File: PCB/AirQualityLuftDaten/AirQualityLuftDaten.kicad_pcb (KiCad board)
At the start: 2 copper layers, 69.9 x 69.9 mm, 21 parts, among them J1 5V_DC_JACK, J10 I2C_2, J11 I2C_3, J12 DHT22, J13 SDS011, J14 ESP_BO1, J15 ESP_BO2, J16 LOGO_LUFTDATEN, J17 LOGO_AirRohr, J18 LOGO_TCEC, J2 5V_POWER, J3 ADC_IN, J4 ADAFRUIT_ADS1115_ADC, J5 PCB, J6 LOGO_OSW, J7 LOGO_TCEC, J8 BME280, J9 I2C_1, P1 5V_USB_Micro, U1 NODEMCU

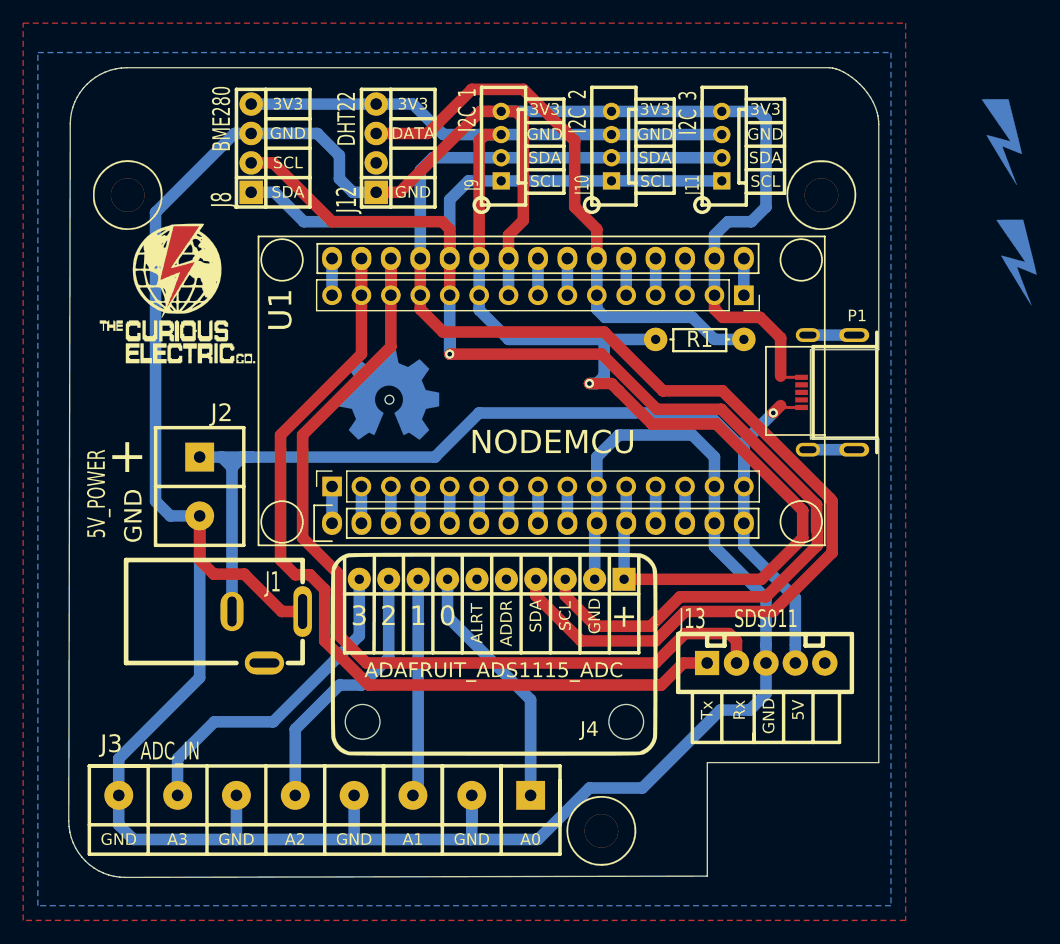
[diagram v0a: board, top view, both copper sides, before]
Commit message: Updated PCB and baseplate files
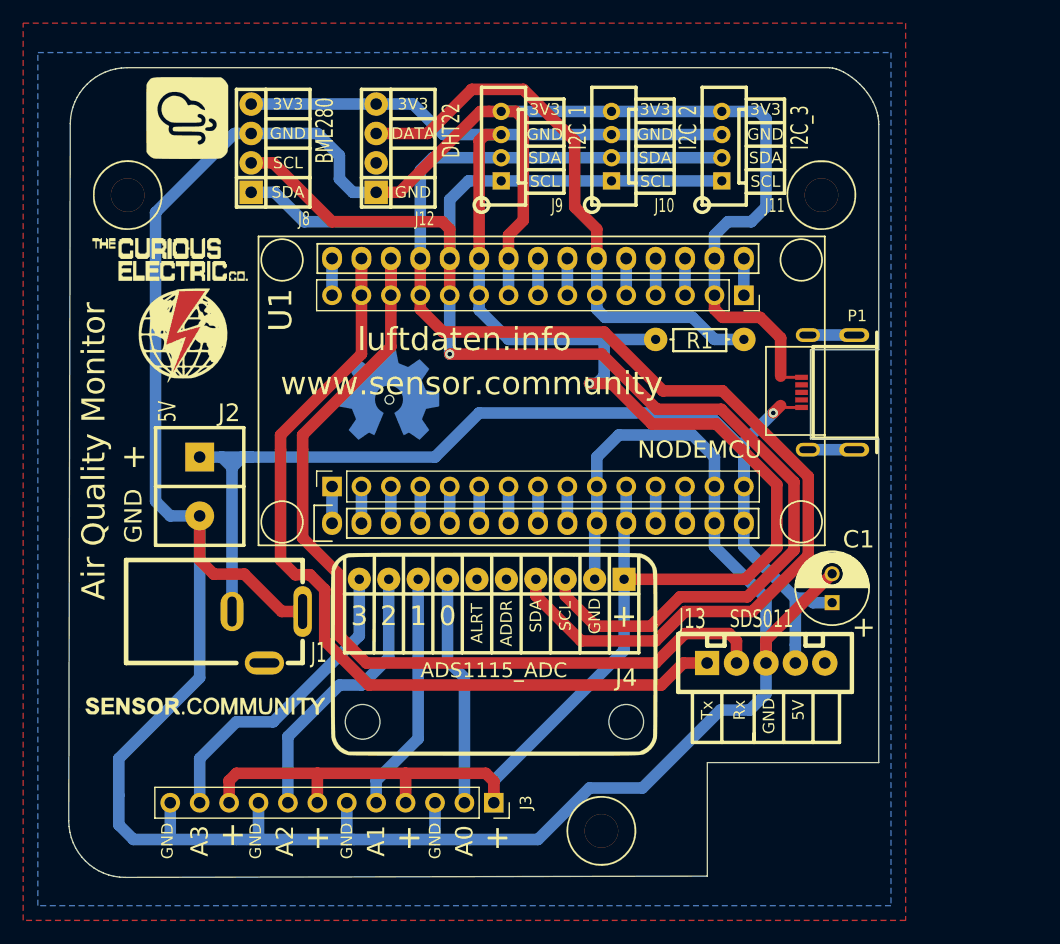
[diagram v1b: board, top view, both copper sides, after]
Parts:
- added C1: 100uf, REInnovationFootprint:C_Radial_D6.3_L11.2_P2.5, F.Cu at (171.4, 105.9)
- J1: value 5V_DC_JACK -> 5V
- J16: footprint CuriousElectric3:2019_011_16_CuriousElectricCompany_Logo_Round_Logo_No_words_KiCAD_10mm_PCBLogo -> CuriousElectric3:sensorcommunity
- J17: footprint CuriousElectric3:2019_011_16_CuriousElectricCompany_Logo_Round_Logo_No_words_KiCAD_10mm_PCBLogo -> CuriousElectric3:logo_conversion
- J2: value 5V_POWER -> 5V
- J3: footprint REInnovationFootprint:SIL_8_Screw_AIO -> REInnovationFootprint:PinSocket_1x12_P2.54mm_Vertical_Labelled
- J4: value ADAFRUIT_ADS1115_ADC -> ADS1115_ADC
- P1: value 5V_USB_Micro -> PWR
- moved J16 82.0 mm to (117.0, 115.2)
- moved J17 72.9 mm to (116.0, 64.0)
- moved J7 7.14 mm to (107.3, 74.2)
- moved J18 5.61 mm to (116.1, 86.9)
- moved J3 3.24 mm to (142.2, 123.2), turned to 270 degrees
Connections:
- J3 pad 1: /A0 -> /PWR_3V3
- J3 pad 2: GND -> /A0
- J3 pad 3: /A1 -> GND
- J3 pad 4: GND -> /PWR_3V3
- J3 pad 5: /A2 -> /A1
- J3 pad 7: /A3 -> /PWR_3V3
- J3 pad 8: GND -> /A2
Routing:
- net /PWR_3V3: track 129.8 -> 183.3 mm
- net GND: track 304.9 -> 313.7 mm
- net +5V: track 96.0 -> 99.4 mm
- net /BME280_SDA: track 132.8 -> 130.0 mm
- net /BME280_SCL: track 129.1 -> 126.5 mm
- net /A1: track 18.8 -> 20.8 mm
- net /A0: track 21.6 -> 19.9 mm
- net /A3: track 28.1 -> 26.9 mm
- net /A2: track 23.1 -> 24.0 mm
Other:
- board text added: "Air Quality Monitor"
- board text added: "PCB by: curiouselectric.co.uk"
- board text added: "luftdaten.info"
- board text added: "www.sensor.community"
